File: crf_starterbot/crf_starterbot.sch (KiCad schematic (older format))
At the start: 9 parts

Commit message: Continued importing from the given schematic
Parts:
- removed SW?: SW_SPDT, symbol Switch:SW_SPDT
- added C?: C_Small, symbol Device:C_Small
- added Q?: Q_NPN_BCE, symbol Device:Q_NPN_BCE
- added R? (x2): DNL/100K, symbol Device:R_Small
- added R?: 0, symbol Device:R_Small
- added R?: 33K, symbol Device:R_Small
- added R? (x2): 10K, symbol Device:R_Small
- added SW? (x2): SW_SPST, symbol Switch:SW_SPST
- added U103: WeMos_D1_mini, Module:WEMOS_D1_mini_light, symbol MCU_Module:WeMos_D1_mini
- added U104: HC-SR04, XCVR_HC-SR04, symbol hr-sc04:HC-SR04
- added U?: L9110, symbol crf_starterbot-rescue:L9110-motordriver
- added U? (x2): E048-03, symbol Isolator:SFH617A-1
- U101: renamed from U?; symbol motordriver:L9110 -> crf_starterbot-rescue:L9110-motordriver
- gave numbers to parts that had none: 5
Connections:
- net labels added: +3V3, +BATT, ECHO, GND, LED, LEFTA, LEFTB, LEFT_ENC, LEFT_SW, RIGHTA, RIGHTB, RIGHT_ENC, RIGHT_SW, TEMP, TRIG
- wire segments 0 -> 55
- no-connect marks 1 -> 2
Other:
- moved on the sheet: J101, J102, J103, TH101, U102A, U102B, U102C

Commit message: Almost completed all essential circuits
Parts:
- removed J101: Screw_Terminal_01x02, symbol Connector:Screw_Terminal_01x02
- removed U101: L9110, symbol crf_starterbot-rescue:L9110-motordriver
- removed unit 1 of U102
- removed U?: E048-03, symbol Isolator:SFH617A-1
- added C101, C102, C106, C107: 100nF, symbol Device:C_Small
- added C103, C104, C108, C109: C_Small, symbol Device:C_Small
- added J103: Screw_Terminal_01x02, symbol Connector:Screw_Terminal_01x02
- added R101, R103, R104, R105, R106, R111, R112, R113, R117, R118, R119, R121, R123, R124: R_Small, symbol Device:R_Small
- added R107, R110, R120, R122: 10k, symbol Device:R_Small
- added unit 1 of U103
- added U106: E048-03, symbol Isolator:SFH617A-1
- added U107: L9110, symbol crf_starterbot-rescue:L9110-motordriver
- U105: renamed from U104; symbol hr-sc04:HC-SR04 -> crf_starterbot-rescue:HC-SR04-hr-sc04
- gave numbers to parts that had none: 12
- renumbered J102 to J101, J103 to J102, U102 to U103, U103 to U104
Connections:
- net +3V3: now also U103.8 (V+), C103.1, C108.1, R101.1, R103.1, R104.1, R107.1, R110.1, R112.2, R113.1, R117.1, R118.1, R120.1, R122.1, R124.2
- net +BATT: now also U102.2 (VCC), U102.3 (VCC), C102.1, C107.1, U107.2 (VCC), U107.3 (VCC)
- net GND: now also U101.2, U101.3, U102.5 (GND), U102.8 (GND), U103.4 (V-), C102.2, C103.2, C104.2, C107.2, C108.2, C109.2, R105.2, R119.2, U106.2, U106.3, U107.5 (GND), U107.8 (GND)
- net LEFTA: now also U102.6 (IA), R110.2
- net LEFTB: now also U102.7 (IB), R107.2
- net LEFT_ENC: now also U103.7, R111.1, R112.1
- net RIGHTA: now also R122.2, U107.6 (IA)
- net RIGHTB: now also R120.2, U107.7 (IB)
- net RIGHT_ENC: now also R123.1, R124.1, U103.1
- net at J101.1 (Pin_1): now also U102.4 (OB), C101.2
- net at J101.2 (Pin_2): now also U102.1 (OA), C101.1
- net at U103.5 (+): now also U101.4, C104.1, R103.2, R111.2
- net at U103.6 (_): now also R106.1
- net at U101.1: now also R101.2
- net LED: no longer names the net of U104.3 (D0)
- new net: C106.2, J103.1 (Pin_1), U107.4 (OB)
- new net: C106.1, J103.2 (Pin_2), U107.1 (OA)
- new net: R104.2, R105.1, R106.2
- new net: R113.2, U106.1
- new net: C109.1, R117.2, R123.2, U103.3 (+), U106.4
- new net: R118.2, R119.1, R121.2
- new net: R121.1, U103.2 (-)
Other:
- moved on the sheet: J101, U102, U103B, U103C

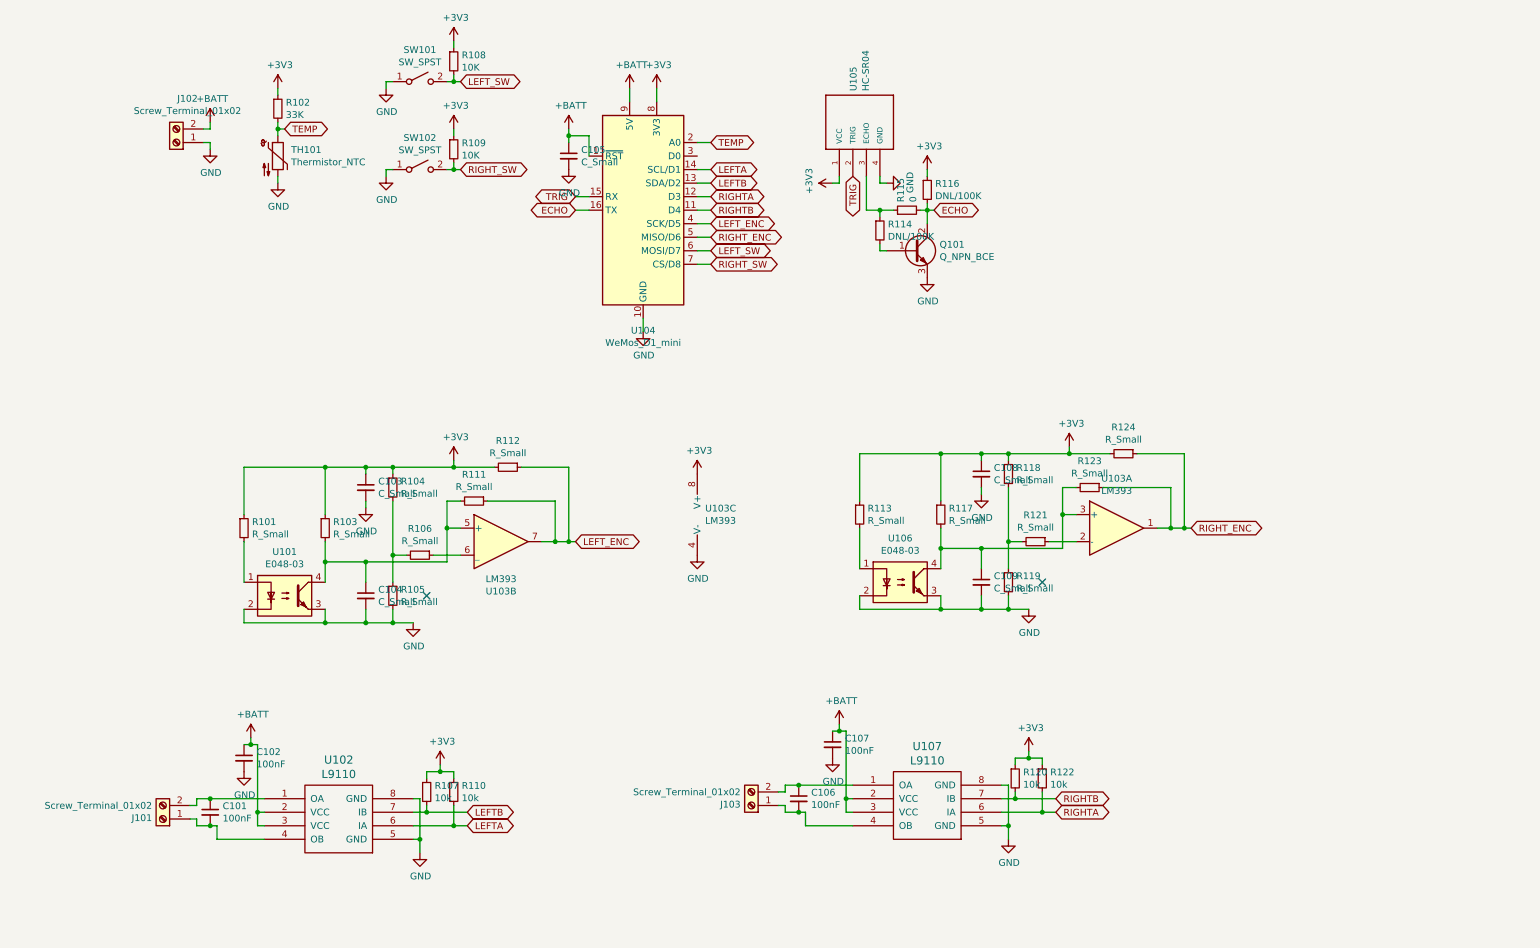
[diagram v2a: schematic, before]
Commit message: basically finished the schematic
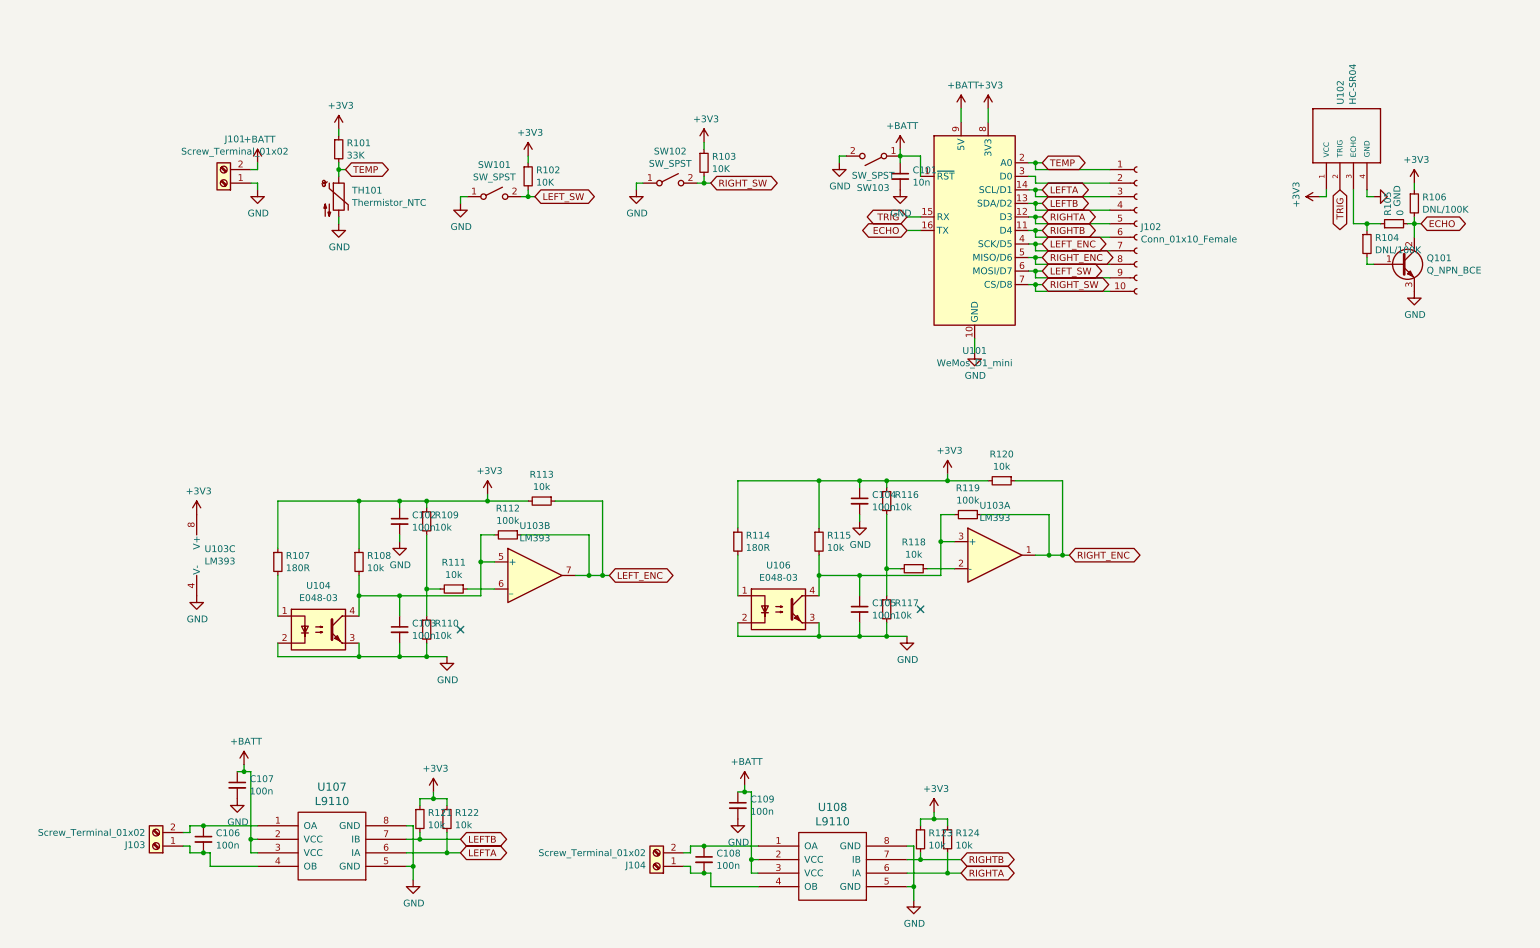
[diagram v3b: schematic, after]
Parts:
- removed C104: C_Small, symbol Device:C_Small
- removed R101, R103, R104, R105, R106: R_Small, symbol Device:R_Small
- removed U101: E048-03, symbol Isolator:SFH617A-1
- added C102: 100n, Capacitor_THT:C_Disc_D5.0mm_W2.5mm_P5.00mm, symbol Device:C_Small
- added J102: Conn_01x10_Female, Connector_PinSocket_2.54mm:PinSocket_1x10_P2.54mm_Horizontal, symbol Connector:Conn_01x10_Female
- added R107: 180R, Resistor_THT:R_Axial_DIN0207_L6.3mm_D2.5mm_P7.62mm_Horizontal, symbol Device:R_Small
- added R108, R109, R110, R113: 10k, Resistor_THT:R_Axial_DIN0207_L6.3mm_D2.5mm_P7.62mm_Horizontal, symbol Device:R_Small
- added SW103: SW_SPST, Button_Switch_THT:SW_PUSH_6mm, symbol Switch:SW_SPST
- added U104: E048-03, Package_DIP:DIP-4_W10.16mm, symbol Isolator:SFH617A-1
- C101: renamed from C105; value C_Small -> 10n; footprint (none) -> Capacitor_THT:C_Disc_D5.0mm_W2.5mm_P5.00mm
- C103: value C_Small -> 100n; footprint (none) -> Capacitor_THT:C_Disc_D5.0mm_W2.5mm_P5.00mm
- C104: renamed from C108; value C_Small -> 100n; footprint (none) -> Capacitor_THT:C_Disc_D5.0mm_W2.5mm_P5.00mm
- C105: renamed from C109; value C_Small -> 100n; footprint (none) -> Capacitor_THT:C_Disc_D5.0mm_W2.5mm_P5.00mm
- C106: renamed from C101; value 100nF -> 100n; footprint (none) -> Capacitor_THT:C_Disc_D5.0mm_W2.5mm_P5.00mm
- C107: renamed from C102; value 100nF -> 100n; footprint (none) -> Capacitor_THT:C_Disc_D5.0mm_W2.5mm_P5.00mm
- C108: renamed from C106; value 100nF -> 100n; footprint (none) -> Capacitor_THT:C_Disc_D5.0mm_W2.5mm_P5.00mm
- C109: renamed from C107; value 100nF -> 100n; footprint (none) -> Capacitor_THT:C_Disc_D5.0mm_W2.5mm_P5.00mm
- J101: renamed from J102; footprint (none) -> TerminalBlock_Phoenix:TerminalBlock_Phoenix_MKDS-1,5-2_1x02_P5.00mm_Horizontal
- J103: renamed from J101; footprint (none) -> TerminalBlock_Phoenix:TerminalBlock_Phoenix_MKDS-1,5-2_1x02_P5.00mm_Horizontal
- J104: renamed from J103; footprint (none) -> TerminalBlock_Phoenix:TerminalBlock_Phoenix_MKDS-1,5-2_1x02_P5.00mm_Horizontal
- Q101: footprint (none) -> Package_TO_SOT_THT:TO-92
- R101: renamed from R102; footprint (none) -> Resistor_THT:R_Axial_DIN0207_L6.3mm_D2.5mm_P7.62mm_Horizontal
- R102: renamed from R108; footprint (none) -> Resistor_THT:R_Axial_DIN0207_L6.3mm_D2.5mm_P7.62mm_Horizontal
- R103: renamed from R109; footprint (none) -> Resistor_THT:R_Axial_DIN0207_L6.3mm_D2.5mm_P7.62mm_Horizontal
- R104: renamed from R114; footprint (none) -> Resistor_THT:R_Axial_DIN0207_L6.3mm_D2.5mm_P7.62mm_Horizontal
- R105: renamed from R115; footprint (none) -> Resistor_THT:R_Axial_DIN0207_L6.3mm_D2.5mm_P7.62mm_Horizontal
- R106: renamed from R116; footprint (none) -> Resistor_THT:R_Axial_DIN0207_L6.3mm_D2.5mm_P7.62mm_Horizontal
- R111: value R_Small -> 10k; footprint (none) -> Resistor_THT:R_Axial_DIN0207_L6.3mm_D2.5mm_P7.62mm_Horizontal
- R112: value R_Small -> 100k; footprint (none) -> Resistor_THT:R_Axial_DIN0207_L6.3mm_D2.5mm_P7.62mm_Horizontal
- R114: renamed from R113; value R_Small -> 180R; footprint (none) -> Resistor_THT:R_Axial_DIN0207_L6.3mm_D2.5mm_P7.62mm_Horizontal
- R115: renamed from R117; value R_Small -> 10k; footprint (none) -> Resistor_THT:R_Axial_DIN0207_L6.3mm_D2.5mm_P7.62mm_Horizontal
- R116: renamed from R118; value R_Small -> 10k; footprint (none) -> Resistor_THT:R_Axial_DIN0207_L6.3mm_D2.5mm_P7.62mm_Horizontal
- R117: renamed from R119; value R_Small -> 10k; footprint (none) -> Resistor_THT:R_Axial_DIN0207_L6.3mm_D2.5mm_P7.62mm_Horizontal
- R118: renamed from R121; value R_Small -> 10k; footprint (none) -> Resistor_THT:R_Axial_DIN0207_L6.3mm_D2.5mm_P7.62mm_Horizontal
- R119: renamed from R123; value R_Small -> 100k; footprint (none) -> Resistor_THT:R_Axial_DIN0207_L6.3mm_D2.5mm_P7.62mm_Horizontal
- R120: renamed from R124; value R_Small -> 10k; footprint (none) -> Resistor_THT:R_Axial_DIN0207_L6.3mm_D2.5mm_P7.62mm_Horizontal
- R121: renamed from R107; footprint (none) -> Resistor_THT:R_Axial_DIN0207_L6.3mm_D2.5mm_P7.62mm_Horizontal
- R122: renamed from R110; footprint (none) -> Resistor_THT:R_Axial_DIN0207_L6.3mm_D2.5mm_P7.62mm_Horizontal
- R123: renamed from R120; footprint (none) -> Resistor_THT:R_Axial_DIN0207_L6.3mm_D2.5mm_P7.62mm_Horizontal
- R124: renamed from R122; footprint (none) -> Resistor_THT:R_Axial_DIN0207_L6.3mm_D2.5mm_P7.62mm_Horizontal
- SW101, SW102: footprint (none) -> Button_Switch_THT:SW_PUSH_6mm
- TH101: footprint (none) -> Resistor_THT:R_Axial_DIN0204_L3.6mm_D1.6mm_P2.54mm_Vertical
- U103: footprint (none) -> Package_DIP:DIP-8_W7.62mm_Socket
- U106: footprint (none) -> Package_DIP:DIP-4_W10.16mm
- U107: renamed from U102; footprint (none) -> Package_DIP:DIP-8_W7.62mm_Socket
- U108: renamed from U107; footprint (none) -> Package_DIP:DIP-8_W7.62mm_Socket
- renumbered U104 to U101, U105 to U102
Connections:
- net +3V3: now also C102.1, R107.1, R108.1, R109.1, R113.2; no longer C103.1, R112.2
- net +BATT: now also SW103.1 (A)
- net GND: now also C102.2, R110.2, SW103.2 (B), U104.2, U104.3
- net LEFTA: now also J102.3 (Pin_3)
- net LEFTB: now also J102.4 (Pin_4)
- net LEFT_ENC: now also J102.7 (Pin_7), R113.1; no longer R111.1
- net LEFT_SW: now also J102.9 (Pin_9)
- net RIGHTA: now also J102.5 (Pin_5)
- net RIGHTB: now also J102.6 (Pin_6)
- net RIGHT_ENC: now also J102.8 (Pin_8)
- net RIGHT_SW: now also J102.10 (Pin_10)
- net TEMP: now also J102.1 (Pin_1)
- net at U103.5 (+): now also C103.1, R112.2, R108.2, U104.4; no longer R111.2
- net at U103.6 (_): now also R111.1
- net at U101.3 (D0): now also J102.2 (Pin_2)
- new net: R107.2, U104.1
- new net: R109.2, R110.1, R111.2
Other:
- moved on the sheet: C101, C104, C105, C106, C107, C108, C109, J101, J103, J104, Q101, R101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
